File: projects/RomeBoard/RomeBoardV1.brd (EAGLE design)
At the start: 110 x 135 mm, 26 parts, among them J1 HEADER-5, J2 RASPBERRY-PI-HEADER, M1 2N7000, M2 2N7000, M3 2N7000

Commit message: Board + Schematic routed
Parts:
- added R8: 10K, passives:AXIAL-0.4
- C1: value 1000uF -> 680uF; device resistor:E7,5-16 -> resistor:E5-10,5
- C2: device resistor:E3,5-10 -> resistor:E5-10,5
- L1: value CTX100-1-52M-R -> 47uH; device BrownSpaceEngineering:CTX100-1-52M-R -> BrownSpaceEngineering:PE-53112NL
- LM2576: value LM2576 -> LM2576HEATSINK; device BrownSpaceEngineering:TO-220-5 -> BrownSpaceEngineering:TO-220-5-HEATSINK
- moved R2 27.8 mm to (87.5, 4.00), turned to 180 degrees
- moved J1 26.0 mm to (98.0, 125.0)
- moved D1 20.7 mm to (43.5, 5.50), turned to 0 degrees
- moved LM2576 20.4 mm to (69.5, 12.0), turned to 90 degrees
- moved R1 20.1 mm to (87.5, 20.0), turned to 0 degrees
- moved L1 17.0 mm to (60.0, 12.0)
- moved V4 8.00 mm to (22.2, 4.94)
- moved V5 8.00 mm to (14.2, 4.94)
- moved C2 6.00 mm to (90.0, 12.0)
- moved C1 4.24 mm to (47.0, 14.0)
- moved R4 2.24 mm to (32.0, 10.0)
- moved D2 2.00 mm to (19.0, 63.0)
- moved D6 2.00 mm to (19.0, 15.0)
- moved M1 2.00 mm to (26.0, 63.0)
- moved R5 2.00 mm to (32.0, 58.0)
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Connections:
- new net 3V3: J2.P1, R8.2
- net !SHDN: now also J2.P15, R8.1
- net 3V6: now also L1.P$2; no longer L1.P$3
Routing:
- net VIN: track 0.00 -> 171.9 mm
- net !SHDN: track 0.00 -> 91.8 mm
- net 3V6: track 0.00 -> 86.7 mm
- net RX_L: track 0.00 -> 71.5 mm, vias 0 -> 1
- net TX_L: track 0.00 -> 67.9 mm, vias 0 -> 1
- net RX_D: track 0.00 -> 46.5 mm, vias 0 -> 1
- net TX_D: track 0.00 -> 38.1 mm
- net N$8: track 0.00 -> 30.4 mm
- net 3V3: track 0.00 -> 28.1 mm
- net N$4: track 0.00 -> 20.1 mm
- net N$9: track 0.00 -> 18.5 mm
- net N$3: track 0.00 -> 18.0 mm
- net N$2: track 0.00 -> 17.0 mm
- net PWR_L: track 0.00 -> 17.0 mm
- net GND: track 0.00 -> 16.5 mm, vias 0 -> 2
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- added copper zone on layer 1, net 3V6
- added copper zone on layer 1, net GND
- added copper zone on layer 16, net GND
- added copper zone on layer 1, net N$1
- added copper zone on layer 1, net VIN
- added copper zone on layer 16, net VIN

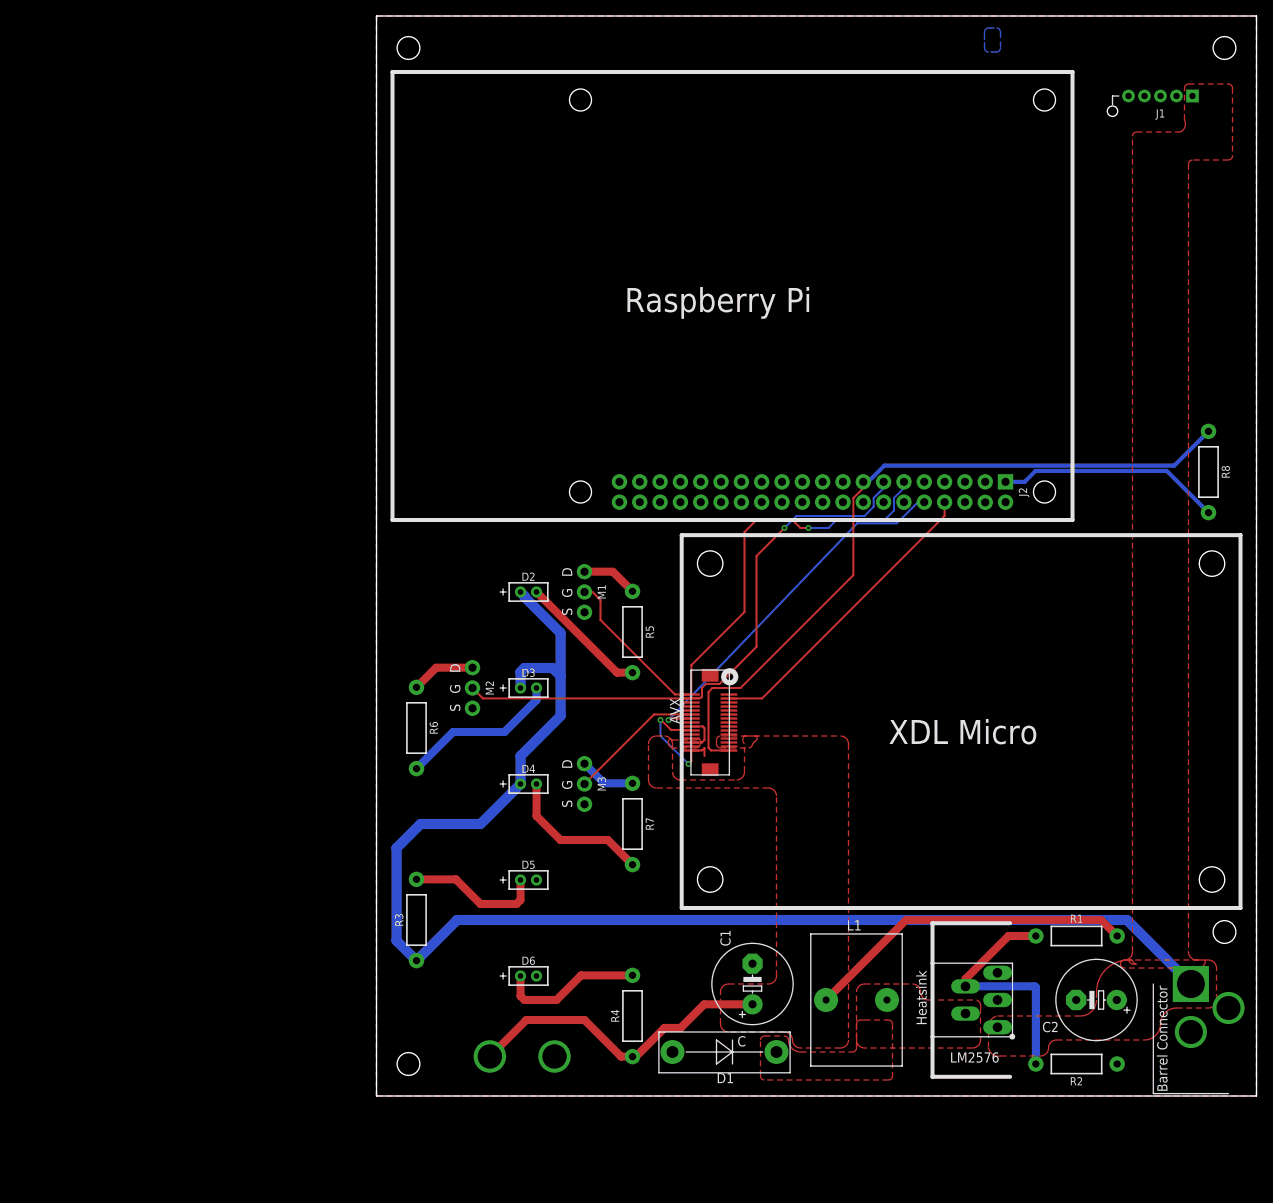
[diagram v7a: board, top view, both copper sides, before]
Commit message: Improved routing, added silkscreen infos
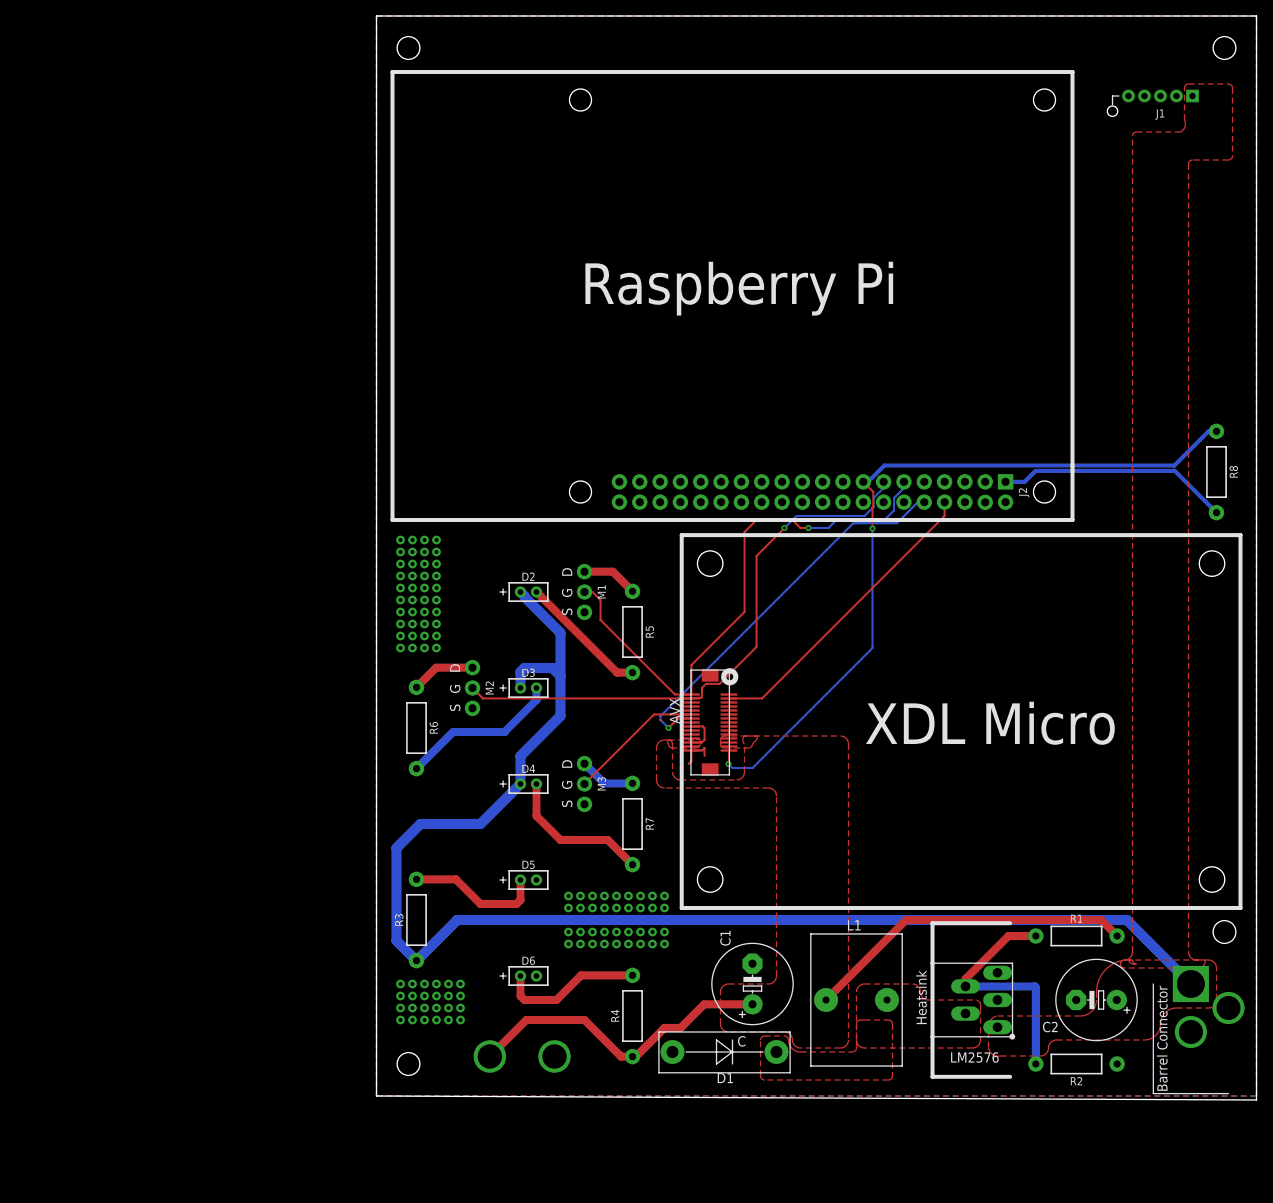
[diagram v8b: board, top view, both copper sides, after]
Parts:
- moved R8 1.00 mm to (105.0, 78.0)
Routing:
- net GND: track 16.5 -> 5.28 mm, vias 2 -> 100
- net RX_D: track 46.5 -> 49.3 mm
- net !SHDN: track 91.8 -> 94.2 mm, vias 0 -> 2
- net 3V3: track 28.1 -> 29.1 mm
- removed copper zone on layer 16, net VIN
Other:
- board size 110 x 135 mm -> 110 x 135.5 mm
- board text added: "3.6V"
- board text added: "5V"
- board text added: "BROWN SPACE ENGINEERING GROUND STATION"
- board text added: "Brown U. Providence, R.I. U.S.A. April 2018"
- board text added: "Che piacere vederti!"
- board text added: "Pi Power"
- board text added: "RX"
- board text added: "Radio Power"
- board text added: "TX"
- board text added: "Viviana Arrunategui Manav Kohli Caelan Ritter"
